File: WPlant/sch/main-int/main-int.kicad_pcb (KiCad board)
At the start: 2 copper layers, 133 parts, among them J1 PROG/JTAG, J10 Ext, J11 HSensor, J12 HSensor, J13 HSensor, J14 HSensor, J15 HSensor, J16 HSensor, J17 HSensor, J18 WaterLevel, J5 220V, J6 Conn_01x08_Pin, J8 eInk-Buttons, J9 Leak, M1 Motor_DC, Q1 FDS9926A, Q2 FDS9926A, Q3 FDS9926A, Q4 FDS9926A, U1 SIWG917Y121MGABAR, U10 SP485EEN-L/TR, U11 TXU0102QDCURQ1, U12 CD74HCT4051M96, U13 CD74HCT4051M96, U14 SN74LVC1G14DBV, U3 AP64352SP-13, U4 AP64352SP-13, U5 TC4427AEOA713, U6 AP2204R-5.0, U7 74HC594, U8 NC7S02P5, U9 INA180A2, X1 SIT1552AI-JE-DCC-32.768D

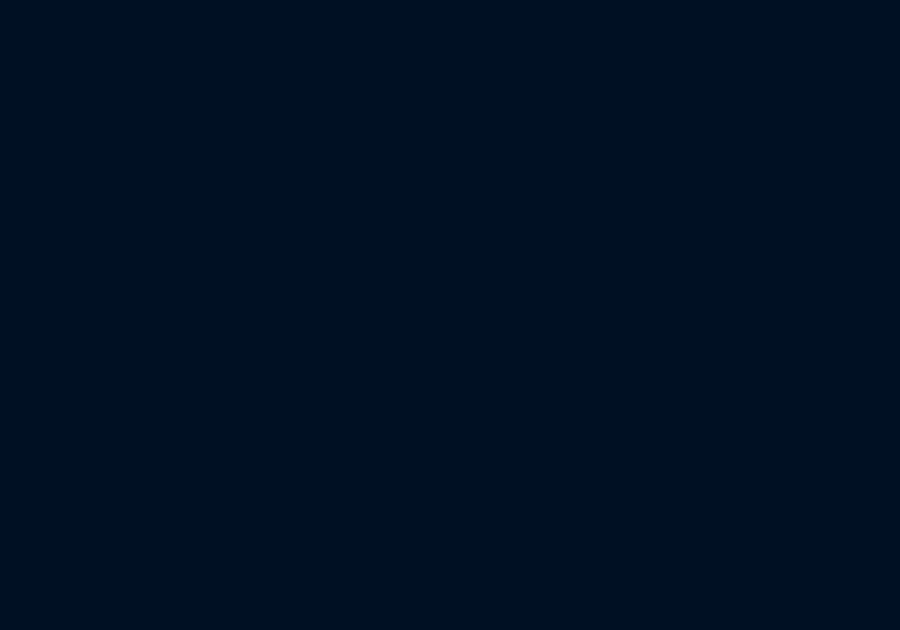
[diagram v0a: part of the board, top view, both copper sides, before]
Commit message: Added jumpers to power lines for Main-* schematics
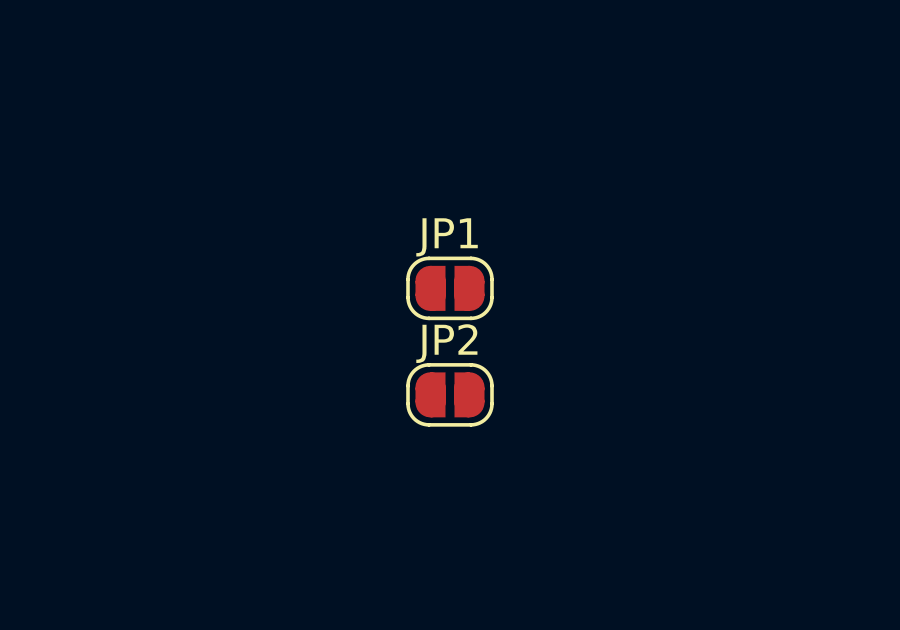
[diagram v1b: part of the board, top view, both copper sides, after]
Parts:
- added JP1: SolderJumper_2_Open, Jumper:SolderJumper-2_P1.3mm_Open_RoundedPad1.0x1.5mm, F.Cu at (159.2, 112.2)
- added JP2: SolderJumper_2_Open, Jumper:SolderJumper-2_P1.3mm_Open_RoundedPad1.0x1.5mm, F.Cu at (159.2, 115.7)
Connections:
- C16 pad 2: +3.3V -> Net-(JP1-A)
- C19 pad 2: +9V -> Net-(JP2-A)
- C20 pad 2: +9V -> Net-(JP2-A)
- C21 pad 2: +9V -> Net-(JP2-A)
- C25 pad 2: +3.3V -> Net-(JP1-A)
- C26 pad 2: +3.3V -> Net-(JP1-A)
- C27 pad 1: +3.3V -> Net-(JP1-A)
- C44 pad 1: +9V -> Net-(JP2-A)
- L2 pad 2: +9V -> Net-(JP2-A)
- L3 pad 2: +3.3V -> Net-(JP1-A)
- R14 pad 1: +9V -> Net-(JP2-A)
- R17 pad 1: +3.3V -> Net-(JP1-A)

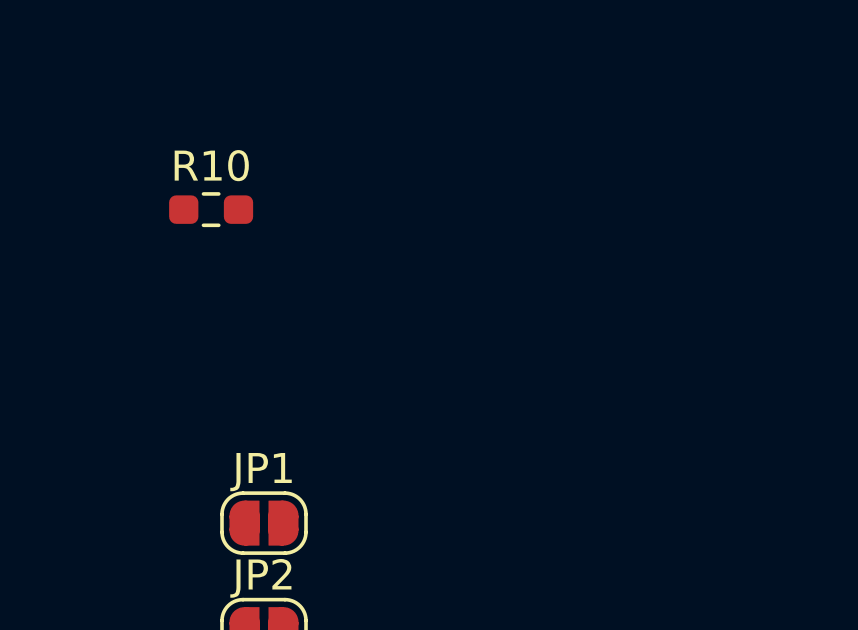
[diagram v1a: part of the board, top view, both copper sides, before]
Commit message: Added more jumpers to power lines for Main-* schematics
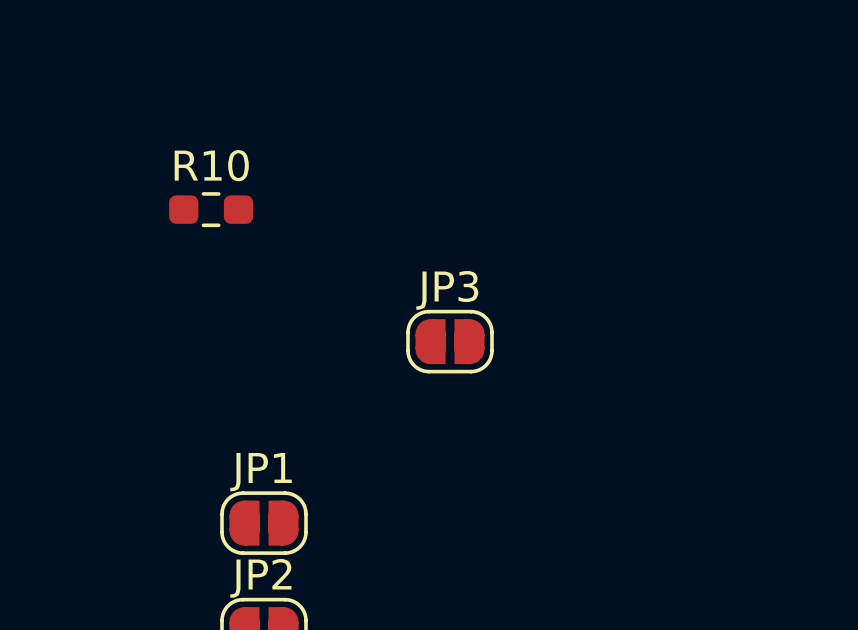
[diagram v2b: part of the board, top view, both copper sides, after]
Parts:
- added JP3: SolderJumper_2_Open, Jumper:SolderJumper-2_P1.3mm_Open_RoundedPad1.0x1.5mm, F.Cu at (165.4, 106.1)
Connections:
- C28 pad 2: +9V -> Net-(JP2-A)
- C29 pad 2: +5V -> Net-(JP3-A)
- C47 pad 1: +5V -> Net-(JP3-A)
- U6 pad 1: +9V -> Net-(JP2-A)
- U6 pad 3: +5V -> Net-(JP3-A)

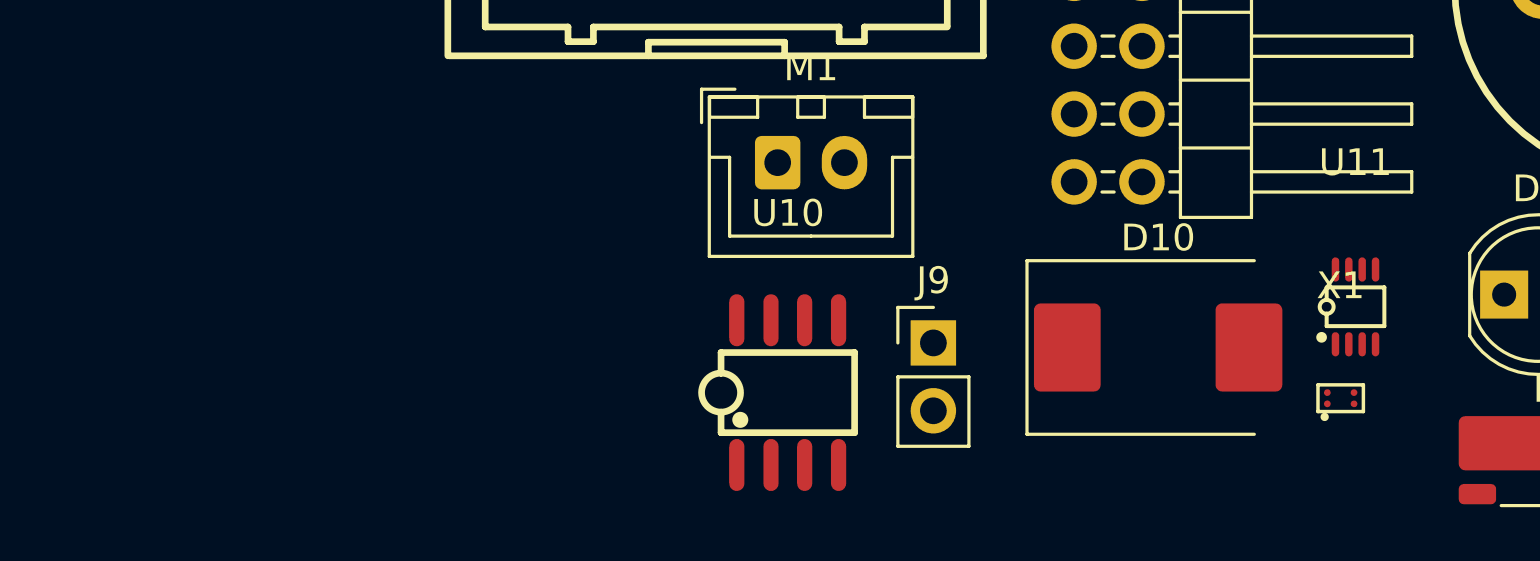
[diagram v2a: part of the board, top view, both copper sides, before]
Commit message: Update SWIG917 footprint. Change footprint of LeakDetector
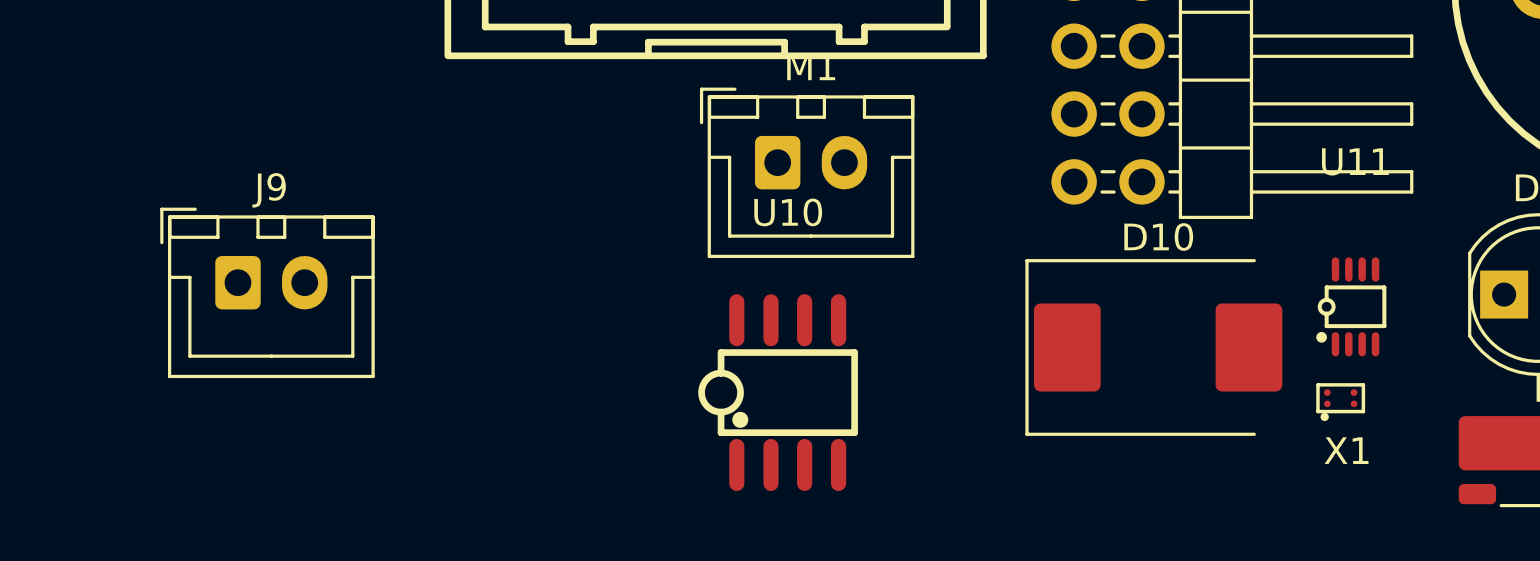
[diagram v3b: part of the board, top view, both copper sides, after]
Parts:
- J9: footprint Connector_PinHeader_2.54mm:PinHeader_1x02_P2.54mm_Vertical -> Connector_JST:JST_XH_B2B-XH-A_1x02_P2.50mm_Vertical
- moved J9 26.1 mm to (80.5, 147.7)

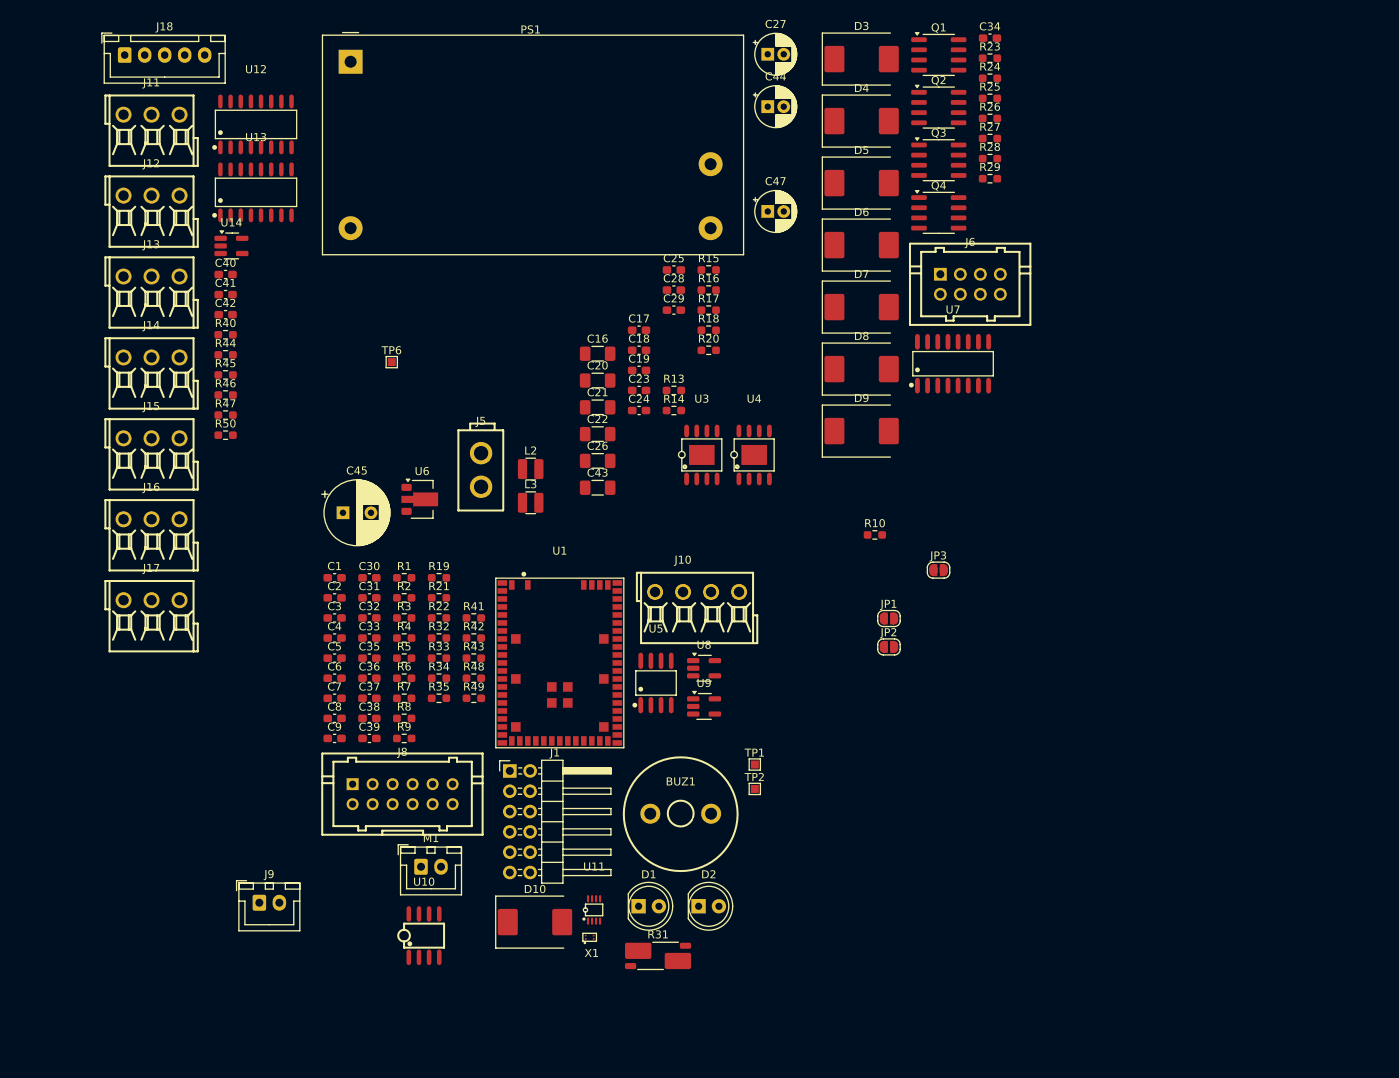
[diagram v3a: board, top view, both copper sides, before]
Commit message: Placement of WP MainInt started
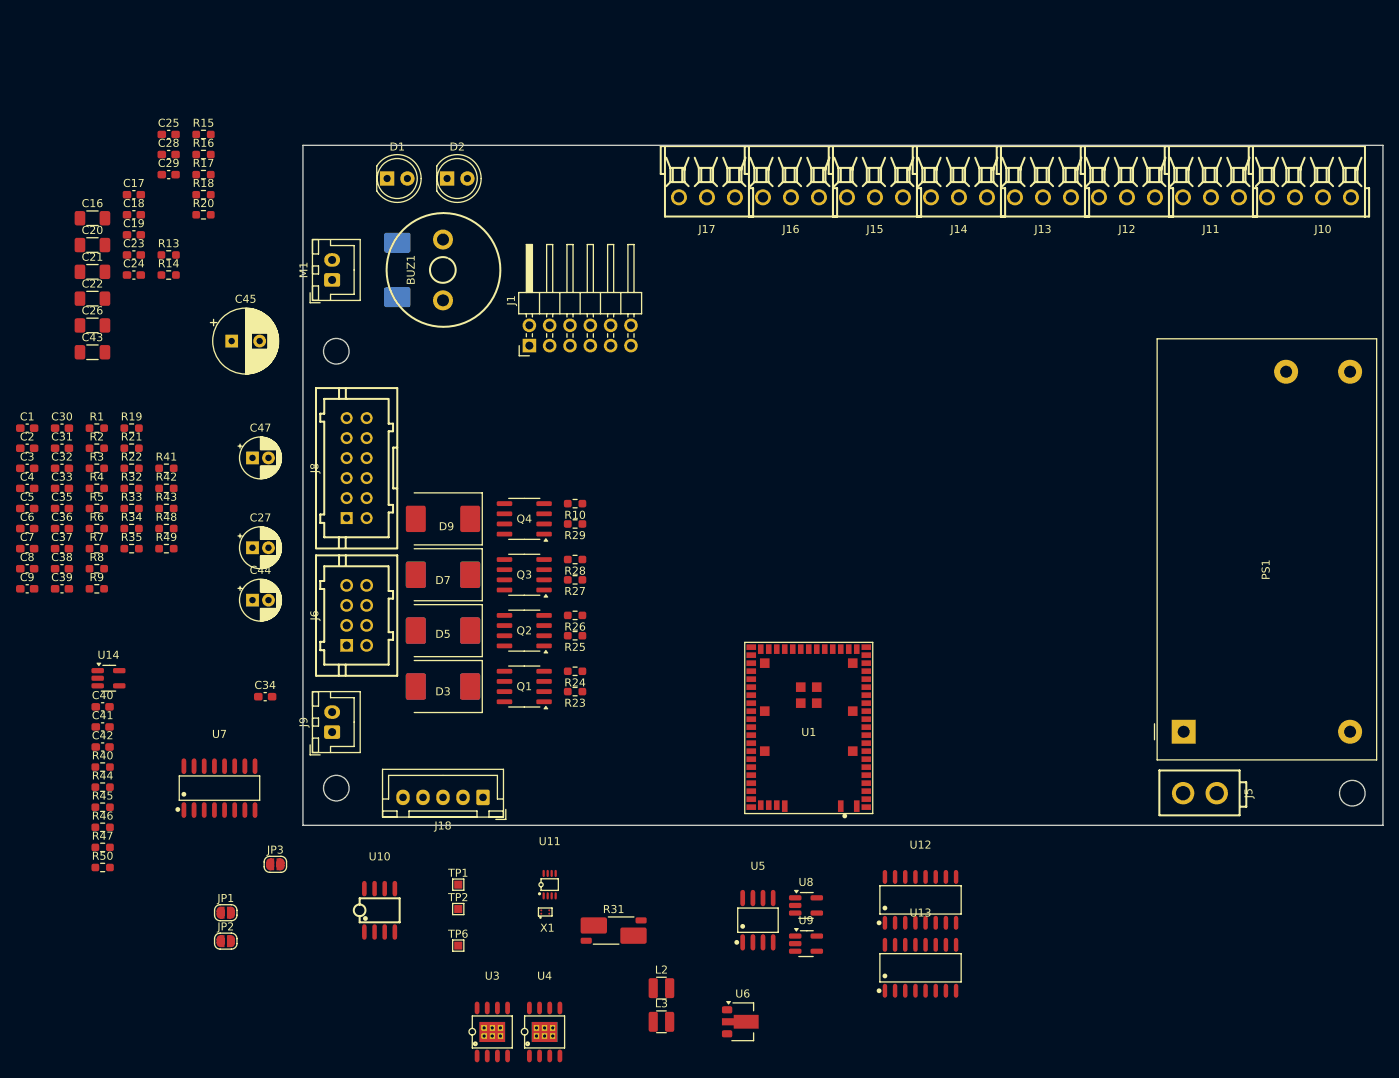
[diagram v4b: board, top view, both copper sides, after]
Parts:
- added REF**: MountingHole_3.2mm_M3, MountingHole:MountingHole_3.2mm_M3, F.Cu at (217.2, 134.0)
- added REF**: MountingHole_3.2mm_M3, MountingHole:MountingHole_3.2mm_M3, F.Cu at (90.2, 78.7)
- added REF**: MountingHole_3.2mm_M3, MountingHole:MountingHole_3.2mm_M3, F.Cu at (90.2, 133.3)
- D10, D4, D6, D8: moved to B.Cu
- U1: footprint easyeda2kicad:COMM-SMD_SIWG917Y110LGNBA -> locals:COMM-SMD_SIWG917Y110LGNBA
- U3, U4: footprint easyeda2kicad:SO-8_L4.9-W3.9-P1.27-LS6.0-BL-EP -> locals:SO-8_L4.9-W3.9-P1.27-LS6.0-BL-EP
- moved PS1 133.6 mm to (196.1, 126.3), turned to 90 degrees
- moved J11 132.8 mm to (199.5, 59.5), turned to 180 degrees
- moved U12 127.7 mm to (163.2, 147.3)
- moved U13 127.7 mm to (163.2, 155.8)
- moved C34 122.4 mm to (81.3, 121.9)
- moved J12 121.9 mm to (189.0, 59.5), turned to 180 degrees
- moved J13 111.9 mm to (178.5, 59.5), turned to 180 degrees
- moved U7 105.9 mm to (75.6, 133.3)
- moved J18 103.0 mm to (108.5, 134.5), turned to 180 degrees
- moved J14 102.9 mm to (168.0, 59.5), turned to 180 degrees
- moved J5 98.5 mm to (198.1, 134.0), turned to -90 degrees
- moved D1 96.3 mm to (96.5, 57.1)
- moved D2 96.3 mm to (104.0, 57.1)
- moved J15 95.3 mm to (157.5, 59.5), turned to 180 degrees
- moved R23 94.6 mm to (120.0, 121.3), turned to 180 degrees
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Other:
- board outline added: 135 x 85 mm

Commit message: Addeed places for latches on Extension board. Updated MainInt sch and pcb
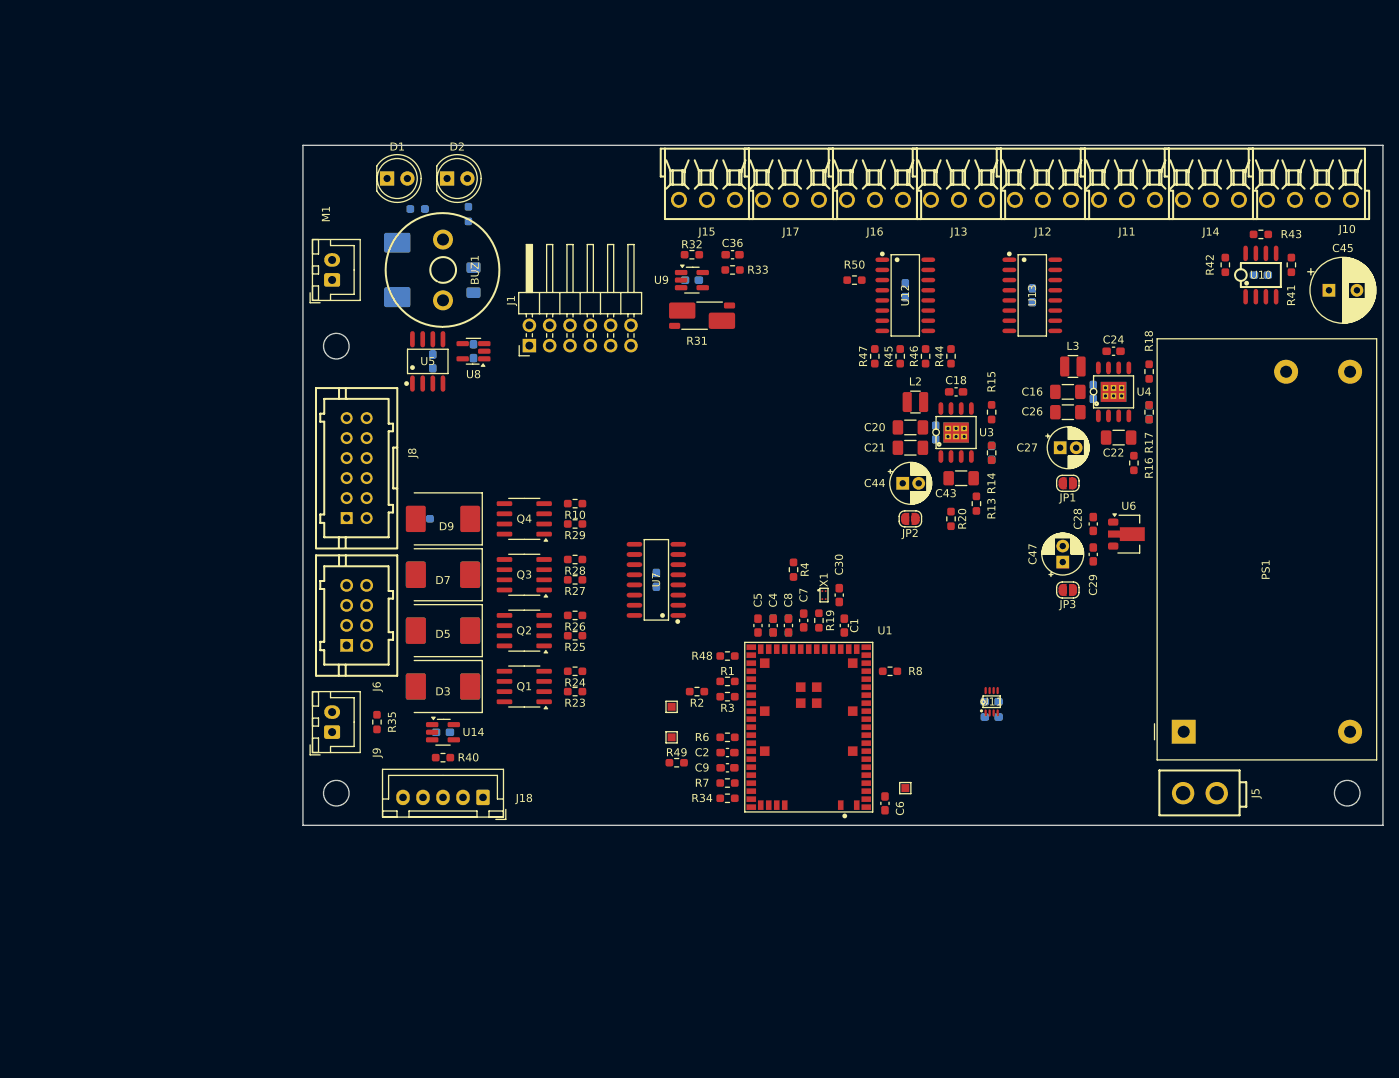
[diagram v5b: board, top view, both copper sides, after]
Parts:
- removed REF** (x3): MountingHole_3.2mm_M3, MountingHole:MountingHole_3.2mm_M3
- added H1: MountingHole, MountingHole:MountingHole_3.2mm_M3, F.Cu at (90.2, 78.1)
- added H2: MountingHole, MountingHole:MountingHole_3.2mm_M3, F.Cu at (216.5, 134.0)
- added H3: MountingHole, MountingHole:MountingHole_3.2mm_M3, F.Cu at (90.2, 134.0)
- C17, C19, C23, C25, C3, C32, C33, C34, C35, C37, C38, C39, C40, C41, C42, R21, R22, R5, R9: moved to B.Cu
- C31: footprint Capacitor_SMD:C_0603_1608Metric_Pad1.08x0.95mm_HandSolder -> Capacitor_SMD:C_1206_3216Metric_Pad1.33x1.80mm_HandSolder; moved to B.Cu
- U1: footprint locals:COMM-SMD_SIWG917Y110LGNBA -> easyeda2kicad:COMM-SMD_SIWG917Y110LGNBA
- moved C37 153.7 mm to (205.7, 69.2)
- moved R41 142.9 mm to (209.6, 67.9), turned to 90 degrees
- moved R43 141.0 mm to (205.7, 64.1)
- moved C45 137.3 mm to (214.2, 71.1)
- moved U10 135.8 mm to (205.7, 69.2)
- moved R42 135.3 mm to (201.3, 67.9), turned to -90 degrees
- moved C22 129.4 mm to (188.0, 89.5), turned to 180 degrees
- moved C41 128.1 mm to (177.2, 71.8), turned to -90 degrees
- moved C25 127.4 mm to (191.8, 86.4), turned to -90 degrees
- moved C29 124.9 mm to (184.8, 104.1), turned to -90 degrees
- moved C28 124.5 mm to (184.8, 100.3), turned to 90 degrees
- moved C16 123.8 mm to (181.6, 83.8), turned to 180 degrees
- moved C24 122.8 mm to (187.3, 78.7)
- moved R16 122.5 mm to (189.9, 92.7), turned to -90 degrees
- moved C26 122.4 mm to (181.6, 86.4), turned to 180 degrees
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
